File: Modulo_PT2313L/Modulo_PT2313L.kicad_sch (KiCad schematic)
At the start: 32 parts, among them J1 Power 9V, J2 LF_Amp, J3 RF_Amp, J4 LR_Amp, J5 RR_Amp, J6 Conn_01x04_Socket, U1 PT2313

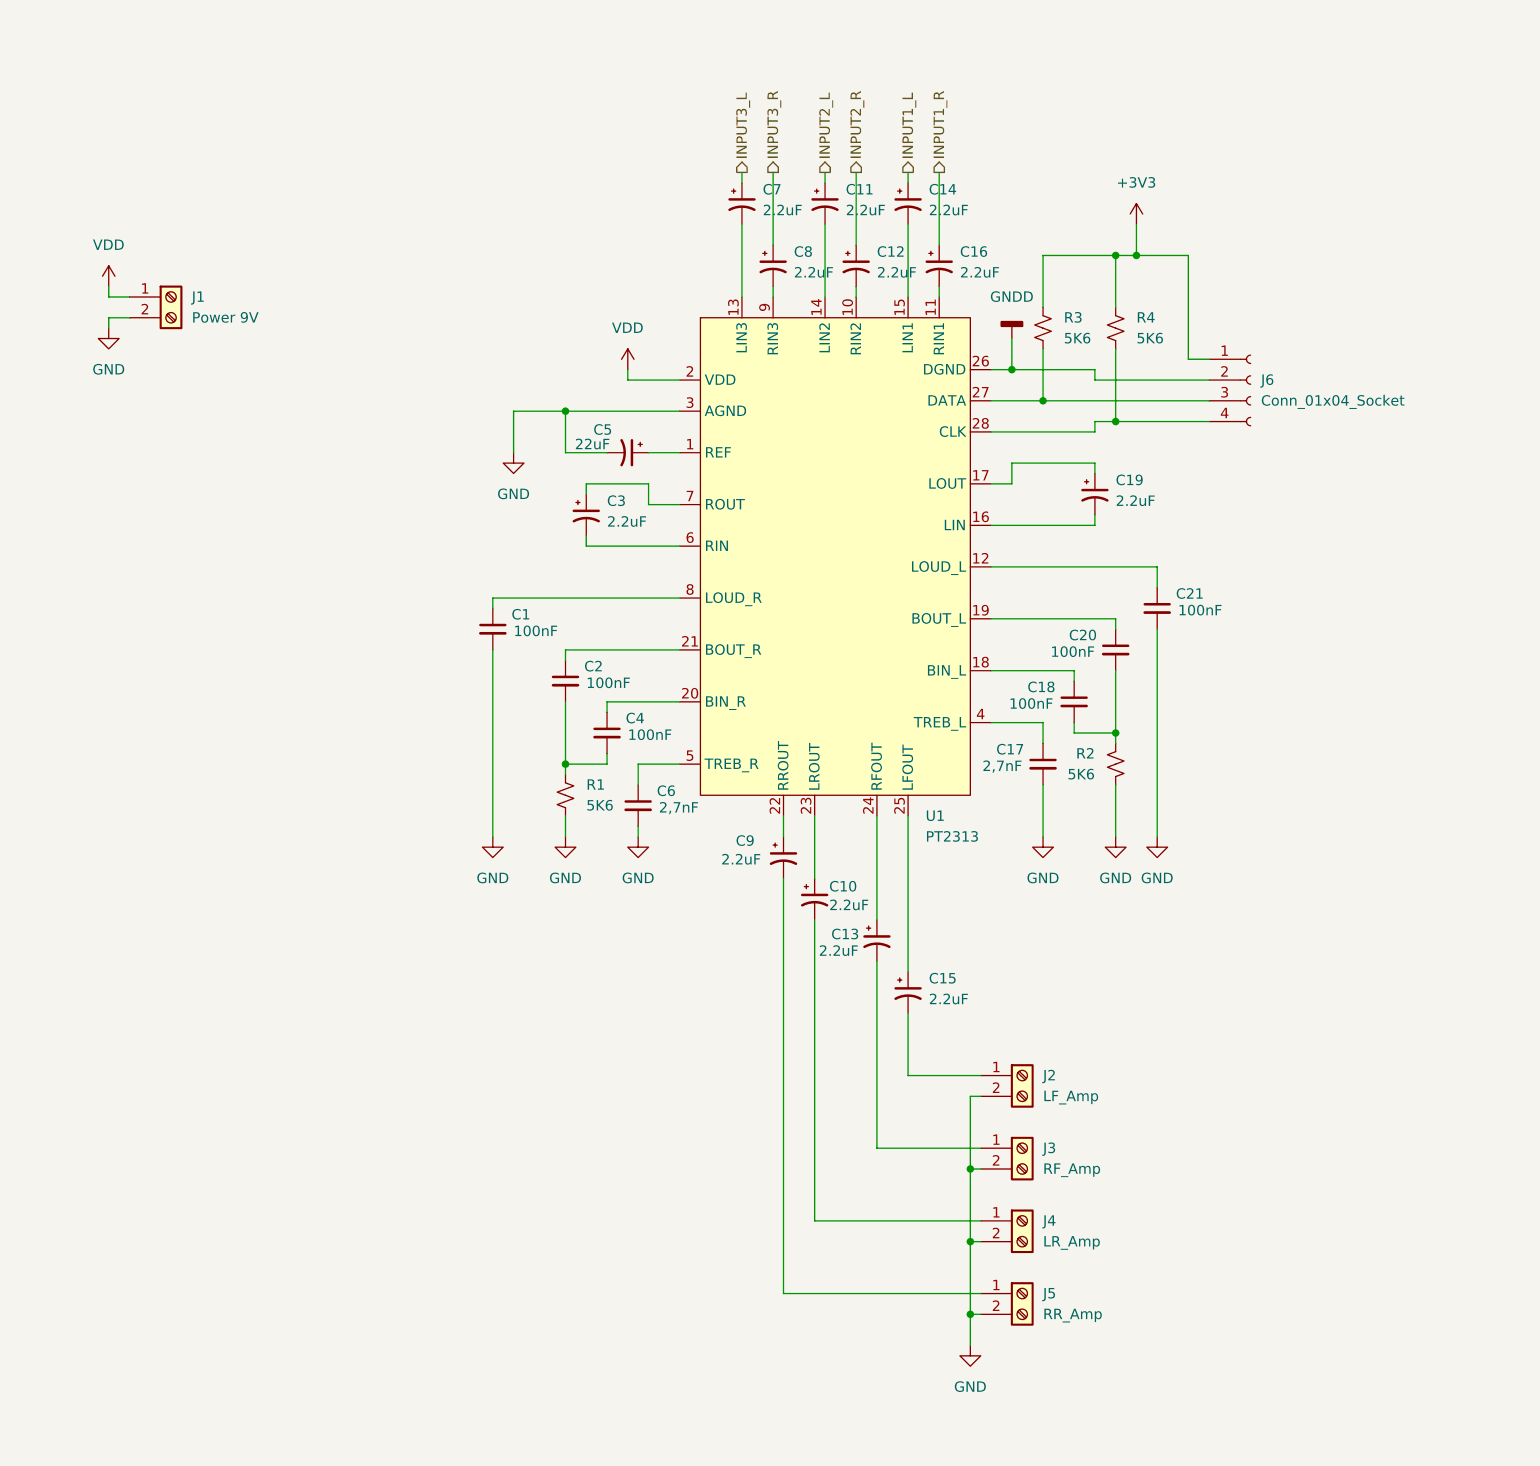
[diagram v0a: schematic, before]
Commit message: agrego imagenes y esquematico
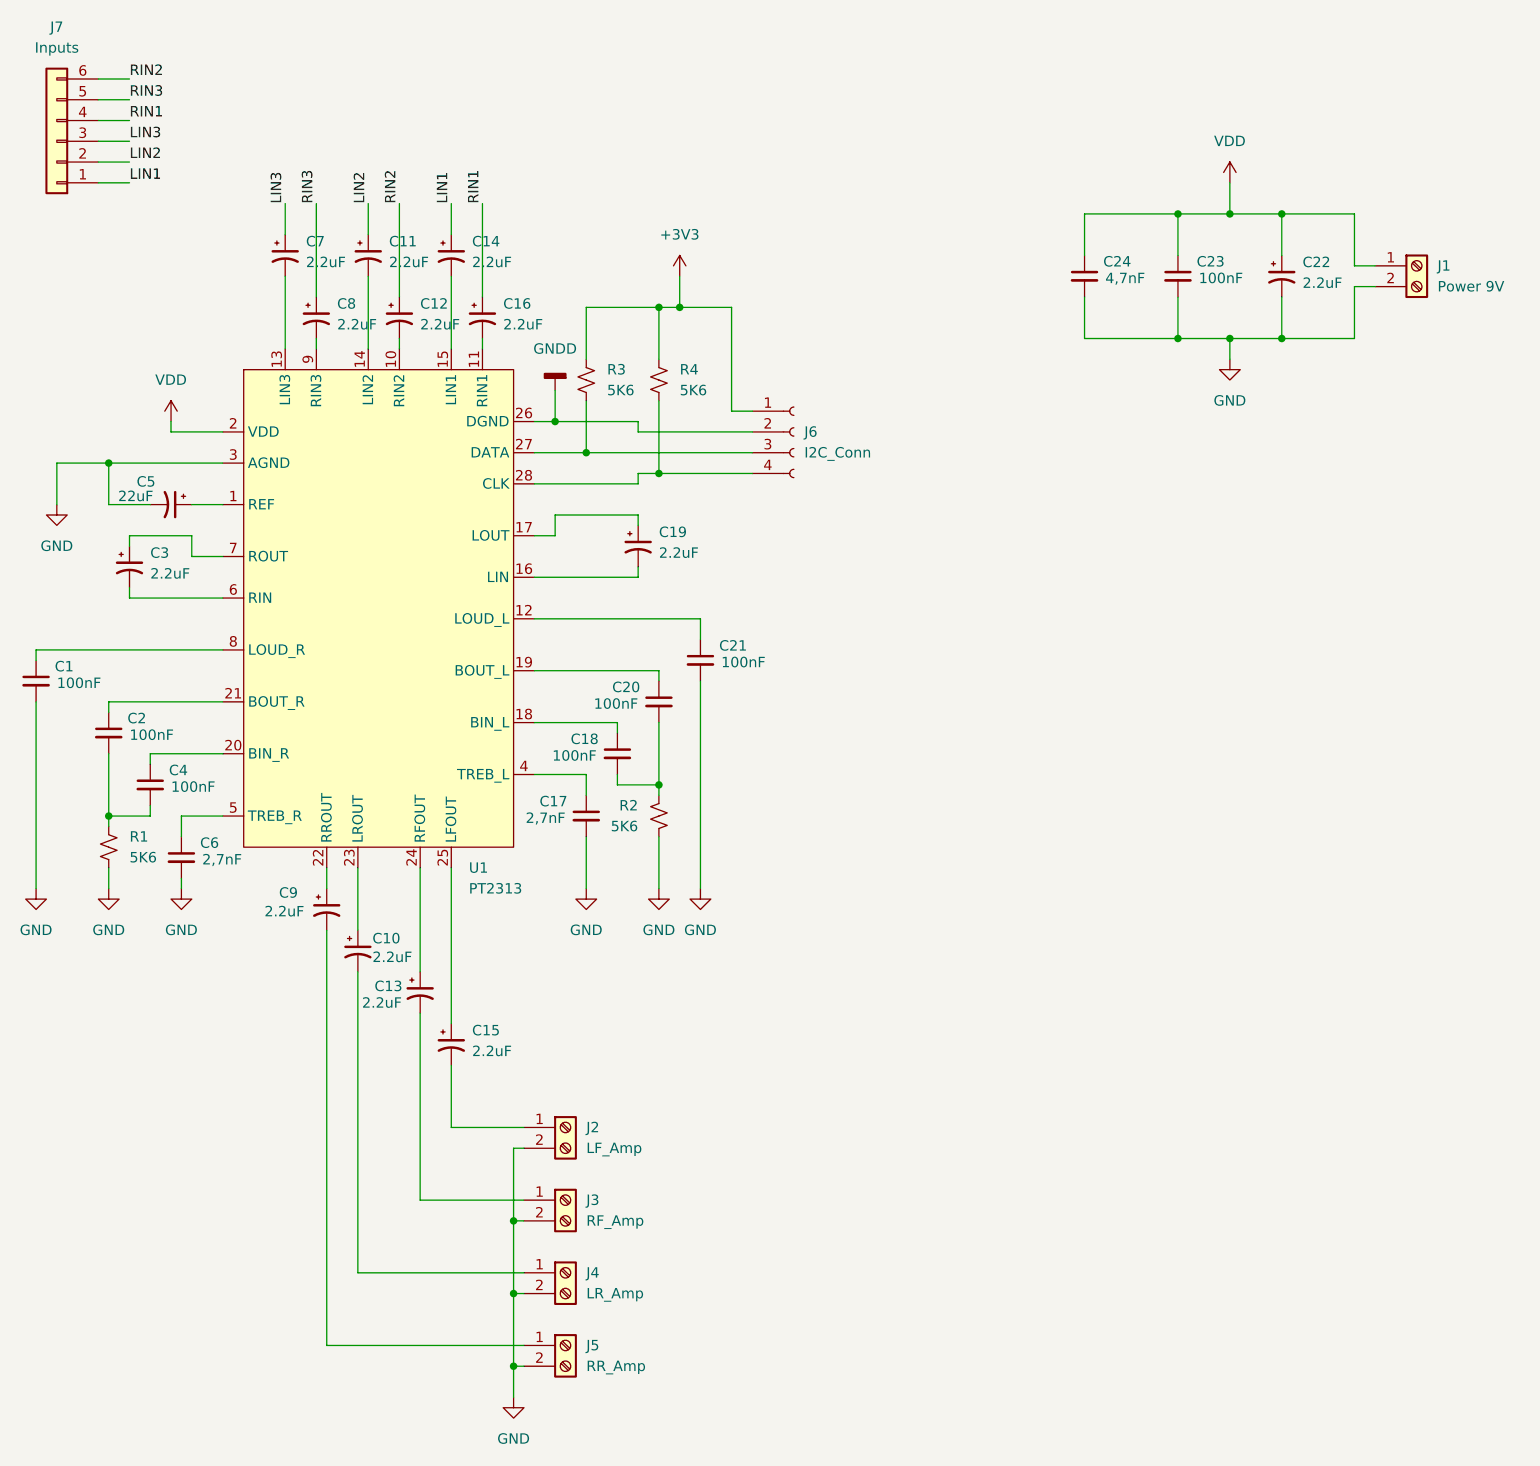
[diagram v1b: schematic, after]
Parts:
- added C22: 2.2uF, Capacitor_THT:CP_Radial_D8.0mm_P2.50mm, symbol Device:C_Polarized_Small_US
- added C23: 100nF, Capacitor_THT:C_Disc_D4.3mm_W1.9mm_P5.00mm, symbol Device:C_Small
- added C24: 4,7nF, Capacitor_THT:C_Rect_L7.0mm_W3.5mm_P5.00mm, symbol Device:C_Small
- added J7: Inputs, Connector_JST:JST_XA_B06B-XASK-1_1x06_P2.50mm_Vertical, symbol Connector_Generic:Conn_01x06
- C21: footprint Capacitor_THT:C_Disc_D4.3mm_W1.9mm_P5.00mm -> Capacitor_THT:C_Disc_D7.5mm_W5.0mm_P10.00mm
- J6: value Conn_01x04_Socket -> I2C_Conn
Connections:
- net GND: now also C22.2, C23.2, C24.2
- net VDD: now also C22.1, C23.1, C24.1
- net INPUT1_L renamed LIN1
- net LIN1: now also J7.1 (Pin_1)
- net INPUT1_R renamed RIN1
- net RIN1: now also J7.4 (Pin_4)
- net INPUT2_L renamed LIN2
- net LIN2: now also J7.2 (Pin_2)
- net INPUT2_R renamed RIN2
- net RIN2: now also J7.6 (Pin_6)
- net INPUT3_L renamed LIN3
- net LIN3: now also J7.3 (Pin_3)
- net INPUT3_R renamed RIN3
- net RIN3: now also J7.5 (Pin_5)
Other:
- company: (none) -> Decima Enrique Emanuel
- title: (none) -> Modulo basado en el IC PT2313L
- moved on the sheet: C1, C10, C11, C12, C13, C14, C15, C16, C17, C18, C19, C2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
